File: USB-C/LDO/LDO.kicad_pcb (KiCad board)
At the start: 4 copper layers, 32 x 84 mm, 32 parts, among them J1 USB_C_Receptacle_PowerOnly_6P, J2 Conn_01x03_Pin, J3 AudioJack2_Ground, J4 AudioJack2_Ground, J5 Conn_02x04_Odd_Even, J6 Conn_02x04_Odd_Even, U1 LM27762, U2 OPA1655

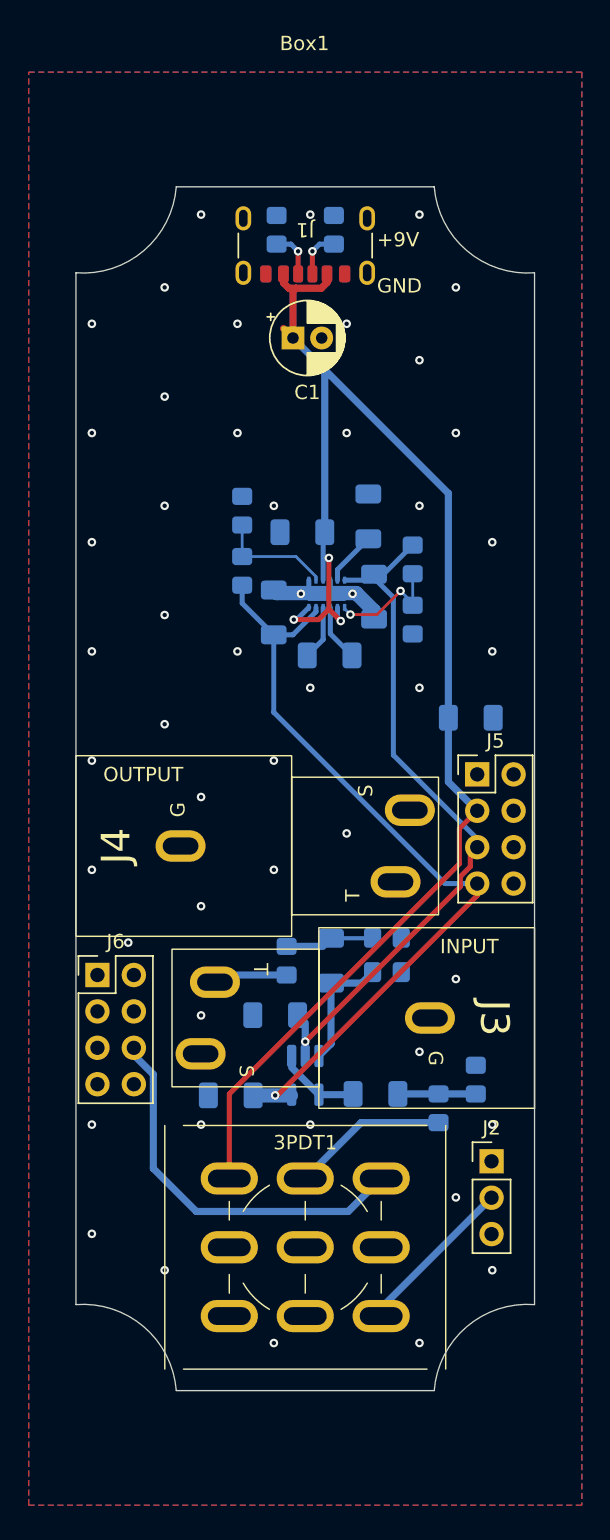
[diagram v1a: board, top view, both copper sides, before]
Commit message: Convert the USB LDO base board and the Octaver to 2-layer boards
I said I wouldn't do this, because 4-layer boards just makes it easier
being lazy, and doesn't involve messing up the gerbers by switching
stack-up in the middle of the project.

But I wanted to see how painful it would be, particularly with the
fairly packed Octaver board (well, packed for _me_, not like it's
actually all that full).

The inner layers were pretty empty anyway, since I tend to try to avoid
via routing and mainly used them for some power routing, and it really
wasn't that much work.

I've switched to the new smaller Murata caps on these boards at the same
time.

Signed-off-by: Linus Torvalds <torvalds@linux-foundation.org>
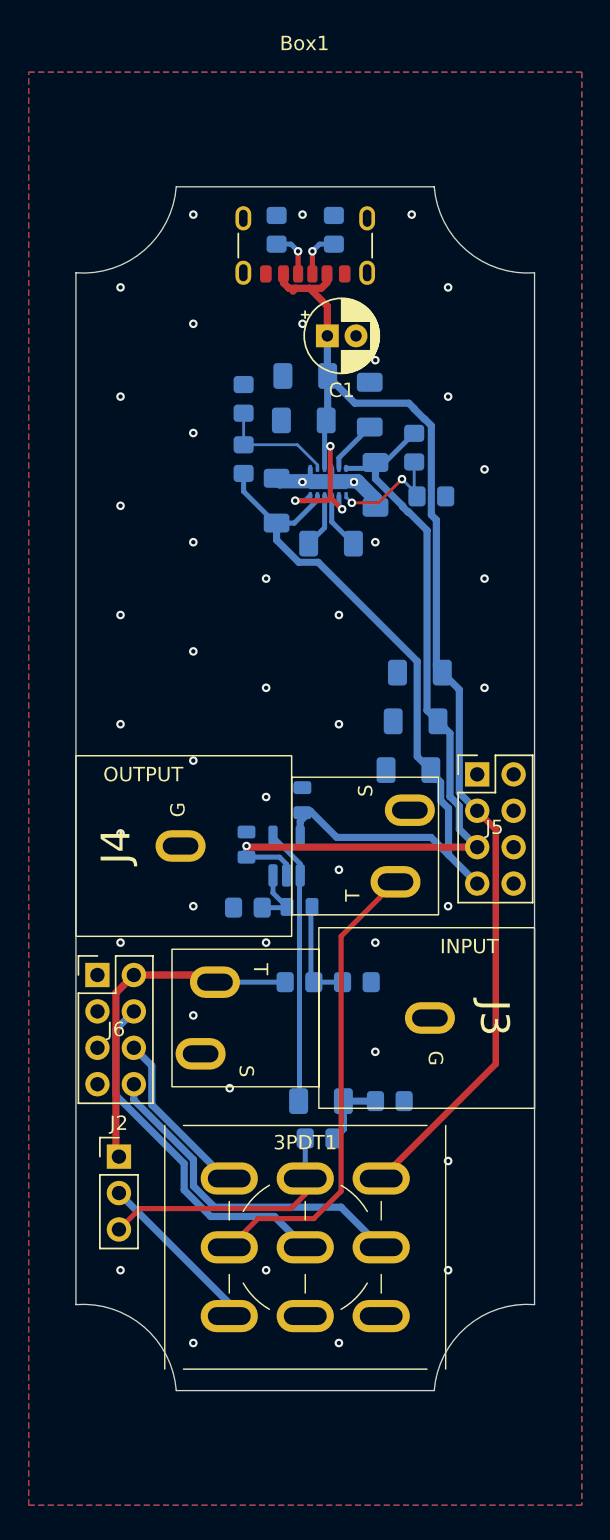
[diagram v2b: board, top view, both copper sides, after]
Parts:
- added C12: 1uF, Capacitor_SMD:C_1206_3216Metric_Pad1.33x1.80mm_HandSolder, B.Cu at (108.0, 91.9)
- added C13: 1uF, Capacitor_SMD:C_1206_3216Metric_Pad1.33x1.80mm_HandSolder, B.Cu at (107.2, 98.7)
- added C14: 1uF, Capacitor_SMD:C_1206_3216Metric_Pad1.33x1.80mm_HandSolder, B.Cu at (107.7, 95.3)
- C10, C11, C9: footprint Capacitor_SMD:C_1206_3216Metric_Pad1.33x1.80mm_HandSolder -> Mylib:C_0704_1810Metric
- moved C4 26.5 mm to (100.0, 71.2), turned to 180 degrees
- moved J2 26.0 mm to (87.0, 125.7)
- moved C10 21.2 mm to (99.8, 100.8), turned to 90 degrees
- moved U2 15.4 mm to (98.7, 104.7), turned to 90 degrees
- moved C11 12.1 mm to (95.9, 103.9), turned to 90 degrees
- moved R11 10.7 mm to (96.0, 108.3), turned to 180 degrees
- moved R4 8.70 mm to (108.8, 79.6), turned to 0 degrees
- moved R7 8.56 mm to (101.0, 124.4), turned to 180 degrees
- moved C3 7.80 mm to (98.0, 79.9)
- moved U1 7.80 mm to (101.6, 78.6)
- moved C2 7.80 mm to (99.9, 74.3)
- moved C5 7.80 mm to (101.8, 82.9)
- moved C6 7.80 mm to (104.9, 78.8)
- moved C7 7.80 mm to (104.5, 73.2)
- moved R1 7.80 mm to (95.7, 77.0)
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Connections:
- 3PDT1 pad 1: VIN -> OUT^{EFF}
- 3PDT1 pad 2: LED -> OUT^{RAW}
- 3PDT1 pad 3: GND -> OUT^{RAW_OR_BUF}
- 3PDT1 pad 7: OUT^{EFF} -> VIN
- 3PDT1 pad 8: OUT^{RAW} -> LED
- 3PDT1 pad 9: OUT^{RAW_OR_BUF} -> GND
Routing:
- net OUT^{EFF}: track 27.3 -> 11.6 mm
- net Net-(U2--): track 5.82 -> 18.9 mm
- net IN^{RAW}: track 34.8 -> 23.0 mm
- net VIN: track 104.7 -> 93.1 mm
- net -V: track 47.3 -> 55.0 mm
- net BUFFERED: track 25.5 -> 17.9 mm
- net LED: track 15.7 -> 23.1 mm
- net OUT^{RAW}: track 27.0 -> 32.6 mm
- net IN: track 8.66 -> 4.18 mm
- net +V: track 56.2 -> 52.9 mm, vias 1 -> 0
- net Net-(C9-Pad1): track 6.20 -> 7.02 mm
- net IN^{EFF}: track 24.5 -> 25.1 mm
- net GND: track 9.92 -> 9.82 mm, vias 49 -> 44
- removed copper zone on In1.Cu, net GND
- removed copper zone on In2.Cu, net GND
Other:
- copper layers 4 -> 2
- board text removed: "+9V GND"

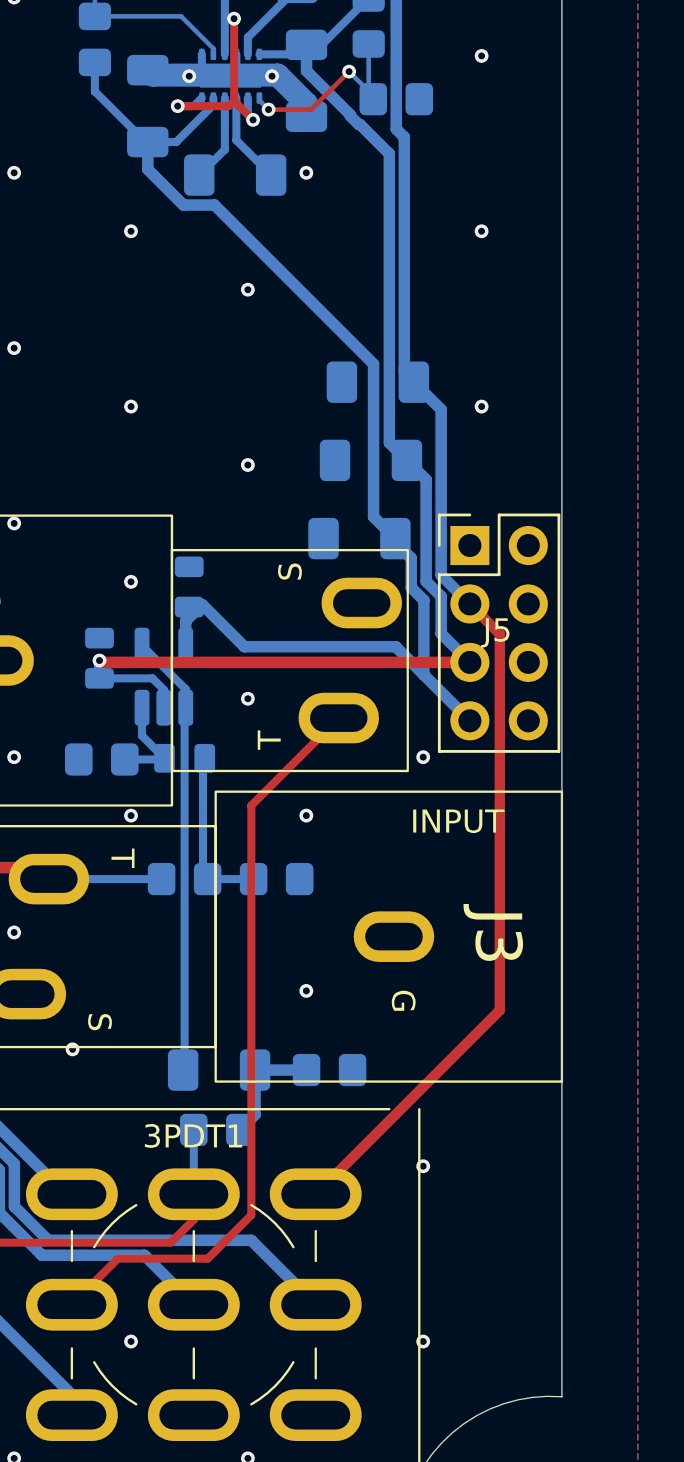
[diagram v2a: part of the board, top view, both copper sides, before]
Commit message: Allow trimming gain on base board input buffer
Instead of just having a unity gain buffer, let's add a trim pot that
allows for higher input gain when that makes sense for the effect board.

For example, the very traditional Big Muff fuzz pedal seems to have an
input stage with roughly a voltage gain of 7x (+17dB).

Random pick: 100k trim pot with 10k resistor gives a gain range of 1-11.

Signed-off-by: Linus Torvalds <torvalds@linux-foundation.org>
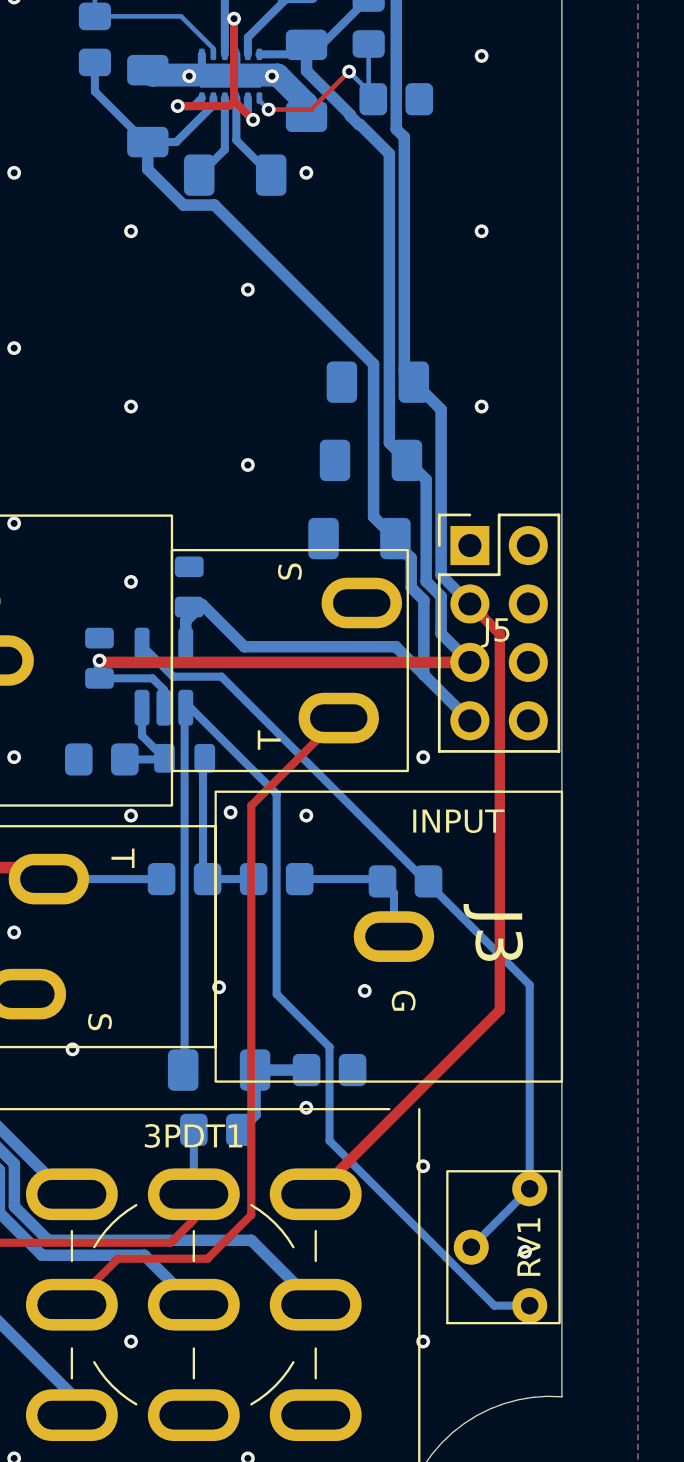
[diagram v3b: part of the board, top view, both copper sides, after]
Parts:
- added R12: 10k, Resistor_SMD:R_0805_2012Metric_Pad1.20x1.40mm_HandSolder, B.Cu at (109.2, 113.6)
- added RV1: 100k, Mylib:Bourns_3362S, F.Cu at (114.6, 129.5)
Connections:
- C8 pad 1: Net-(U2--) -> Net-(C8-Pad1)
- U2 pad 1: Net-(U2--) -> Net-(C8-Pad1)
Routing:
- net Net-(C8-Pad1): track 0.00 -> 48.8 mm
- net Net-(U2--): track 18.9 -> 35.4 mm
- net GND: track 9.82 -> 15.9 mm, vias 44 -> 47
